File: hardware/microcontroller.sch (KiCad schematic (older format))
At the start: 13 parts, among them U4 STM32F411CEUx, Y1 12MHz

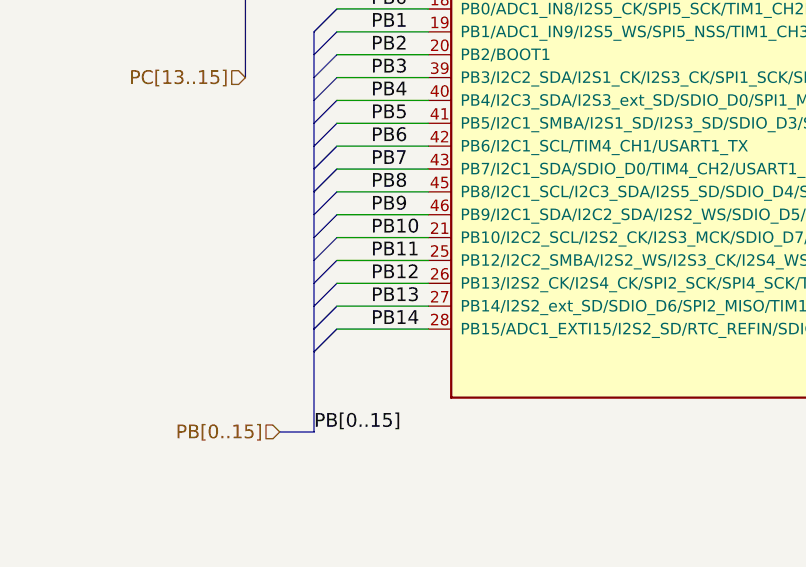
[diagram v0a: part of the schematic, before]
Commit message: Modify the schematic and PCB. At this stage the pinout should be considered and very careful selection of which peripheral goes where needs to be done.
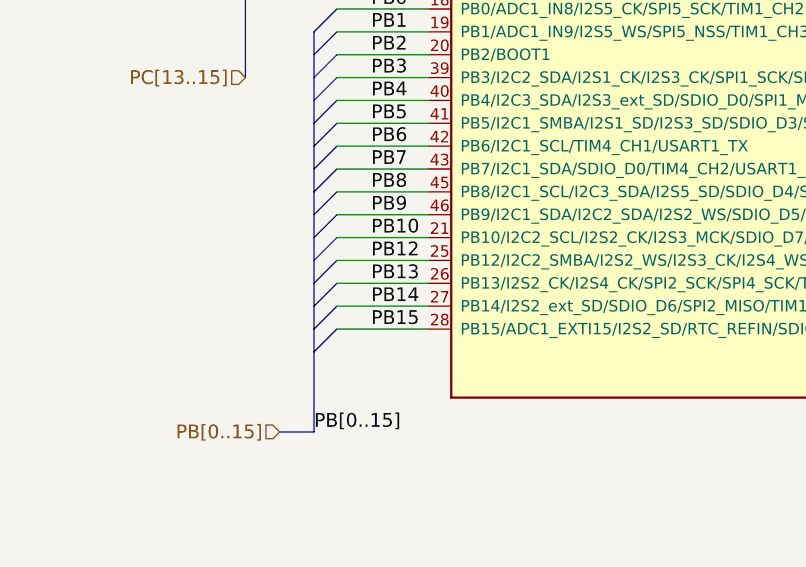
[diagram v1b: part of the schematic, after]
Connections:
- net labels added: PB15
- net labels removed: PB11
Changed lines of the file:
@@
 PB10
 Text Label 2050 4500 0    60   ~ 0
-PB11
+PB12
 Text Label 2050 4600 0    60   ~ 0
-PB12
+PB13
 Text Label 2050 4700 0    60   ~ 0
-PB13
+PB14
 Text Label 2050 4800 0    60   ~ 0
-PB14
+PB15
 Wire Bus Line
 	1800 5250 1650 5250

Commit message: Layed board out for the third time. Doesn't include power traces yet.
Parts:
- U4: footprint Housings_DFN_QFN:QFN-48-1EP_7x7mm_Pitch0.5mm -> Housings_QFP:TQFP-48_7x7mm_Pitch0.5mm
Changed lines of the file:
@@
 EESchema Schematic File Version 2
+LIBS:power
+LIBS:device
+LIBS:transistors
+LIBS:conn
+LIBS:linear
+LIBS:regul
+LIBS:74xx
+LIBS:cmos4000
+LIBS:adc-dac
+LIBS:memory
+LIBS:xilinx
+LIBS:microcontrollers
+LIBS:dsp
+LIBS:microchip
+LIBS:analog_switches
+LIBS:motorola
+LIBS:texas
+LIBS:intel
+LIBS:audio
+LIBS:interface
+LIBS:digital-audio
+LIBS:philips
+LIBS:display
+LIBS:cypress
+LIBS:siliconi
+LIBS:opto
+LIBS:atmel
+LIBS:contrib
+LIBS:valves
+LIBS:stm32
+LIBS:switches
 LIBS:parts
 LIBS:minibot-cache
@@
 $Descr A4 11693 8268
 encoding utf-8
-Sheet 2 5
+Sheet 2 4
 Title "MiniBot"
 Date "2017-06-23"
@@
 F 0 "U4" H 2400 5225 50  0000 L BNN
 F 1 "STM32F411CEUx" H 9600 5225 50  0000 R BNN
-F 2 "Housings_DFN_QFN:QFN-48-1EP_7x7mm_Pitch0.5mm" H 9600 5175 50  0001 R TNN
+F 2 "Housings_QFP:TQFP-48_7x7mm_Pitch0.5mm" H 9600 5175 50  0001 R TNN
 F 3 "" H 6000 3400 50  0001 C CNN
 	1    6000 3400
@@
 $EndComp
 $Comp
-L GND #PWR041
+L GND #PWR025
 U 1 1 59427B2A
 P 1200 2350
-F 0 "#PWR041" H 1200 2100 50  0001 C CNN
+F 0 "#PWR025" H 1200 2100 50  0001 C CNN
 F 1 "GND" V 1200 2150 50  0000 C CNN
 F 2 "" H 1200 2350 50  0001 C CNN
@@
 $EndComp
 $Comp
-L GND #PWR042
+L GND #PWR026
 U 1 1 59427B30
 P 6000 5350
-F 0 "#PWR042" H 6000 5100 50  0001 C CNN
+F 0 "#PWR026" H 6000 5100 50  0001 C CNN
 F 1 "GND" H 6000 5200 50  0000 C CNN
 F 2 "" H 6000 5350 50  0001 C CNN
@@
 $EndComp
 $Comp
-L GND #PWR043
+L GND #PWR027
 U 1 1 59427B60
 P 5150 6850
-F 0 "#PWR043" H 5150 6600 50  0001 C CNN
+F 0 "#PWR027" H 5150 6600 50  0001 C CNN
 F 1 "GND" H 5150 6700 50  0000 C CNN
 F 2 "" H 5150 6850 50  0001 C CNN
@@
 Connection ~ 1350 3100
 $Comp
-L GND #PWR044
+L GND #PWR028
 U 1 1 59427C13
 P 1150 2900
-F 0 "#PWR044" H 1150 2650 50  0001 C CNN
+F 0 "#PWR028" H 1150 2650 50  0001 C CNN
 F 1 "GND" V 1250 2850 50  0000 C CNN
 F 2 "" H 1150 2900 50  0001 C CNN
@@
 $EndComp
 $Comp
-L GND #PWR045
+L GND #PWR029
 U 1 1 59427C19
 P 1550 2900
-F 0 "#PWR045" H 1550 2650 50  0001 C CNN
+F 0 "#PWR029" H 1550 2650 50  0001 C CNN
 F 1 "GND" V 1450 2850 50  0000 C CNN
 F 2 "" H 1550 2900 50  0001 C CNN
@@
 	1050 2700 2300 2700
 $Comp
-L GND #PWR046
+L GND #PWR030
 U 1 1 59427C31
 P 800 2900
-F 0 "#PWR046" H 800 2650 50  0001 C CNN
+F 0 "#PWR030" H 800 2650 50  0001 C CNN
 F 1 "GND" V 800 2700 50  0000 C CNN
 F 2 "" H 800 2900 50  0001 C CNN
@@
 $EndComp
 $Comp
-L GND #PWR047
+L GND #PWR031
 U 1 1 5942944C
 P 2100 6950
-F 0 "#PWR047" H 2100 6700 50  0001 C CNN
+F 0 "#PWR031" H 2100 6700 50  0001 C CNN
 F 1 "GND" H 2100 6800 50  0000 C CNN
 F 2 "" H 2100 6950 50  0001 C CNN
@@
 PC[13..15]
 $Comp
-L +3V3 #PWR048
+L +3V3 #PWR032
 U 1 1 59492047
 P 6000 1400
-F 0 "#PWR048" H 6000 1250 50  0001 C CNN
+F 0 "#PWR032" H 6000 1250 50  0001 C CNN
 F 1 "+3V3" H 6000 1540 50  0000 C CNN
 F 2 "" H 6000 1400 50  0001 C CNN
@@
 $EndComp
 $Comp
-L +3V3 #PWR049
+L +3V3 #PWR033
 U 1 1 59492080
 P 5150 6450
-F 0 "#PWR049" H 5150 6300 50  0001 C CNN
+F 0 "#PWR033" H 5150 6300 50  0001 C CNN
 F 1 "+3V3" H 5150 6590 50  0000 C CNN
 F 2 "" H 5150 6450 50  0001 C CNN
@@
 $EndComp
 $Comp
-L +3V3 #PWR050
+L +3V3 #PWR034
 U 1 1 594920B2
 P 1850 2200
-F 0 "#PWR050" H 1850 2050 50  0001 C CNN
+F 0 "#PWR034" H 1850 2050 50  0001 C CNN
 F 1 "+3V3" H 1850 2340 50  0000 C CNN
 F 2 "" H 1850 2200 50  0001 C CNN
